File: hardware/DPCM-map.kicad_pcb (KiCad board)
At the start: 2 copper layers, 178 x 178 mm, 99 parts, among them J1 JMP, J2 Conn_01x06_Male, J3 Touch_Pad_+, J4 Touch_Pad_0, J5 Touch_Pad_-, J6 JMP, J7 SSD1306, P1 USB_C_Plug, Q1 2N7002, Q2 2N7002, SW1 SW_Push, SW2 SW_+_Fb, SW3 SW_0_Fb, SW4 SW_-_Fb, U1 AZ1117-3.3, U2 BME280, U4 ESP32-WROOM-32, U5 CH340G, Y1 12MHz

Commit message: routing optimization
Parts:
- moved R4 18.3 mm to (186.8, 180.5)
- moved C23 3.62 mm to (180.7, 70.0), turned to 270 degrees
- moved C37 0.28 mm to (157.6, 167.7), turned to 180 degrees
- turned R5 to 180 degrees
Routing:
- net LDR: track 105.3 -> 80.8 mm, vias 1 -> 2
- net +3V3: track 288.5 -> 269.0 mm
- net GND: track 98.2 -> 114.8 mm, vias 25 -> 40
- net SDA: track 181.4 -> 178.4 mm, vias 2 -> 4
- net LED_CHAIN: track 87.9 -> 90.4 mm
- net +5V: track 588.2 -> 585.8 mm, vias 0 -> 9
- net SCL: track 183.9 -> 182.0 mm
- net TOUCH_0: track 139.3 -> 141.0 mm
- net TOUCH_+: track 189.5 -> 191.1 mm
- net WIFI_RESET: track 60.3 -> 61.8 mm
- net Net-(D7-Pad2): track 18.8 -> 19.9 mm
- net RX: track 116.1 -> 115.2 mm
- net BOOT0: track 85.2 -> 86.1 mm
- net Net-(D19-Pad2): track 27.1 -> 26.4 mm, vias 0 -> 2
- net Net-(D22-Pad2): track 72.0 -> 72.2 mm, vias 0 -> 2
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
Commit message: move oled, change tracks
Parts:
- added G***: LOGO, map_edges_keepout:oled_display, F.Cu at (170.3, 211.3)
- moved J7 106.7 mm to (166.4, 199.1), turned to 270 degrees
- moved JP3 101.8 mm to (169.0, 194.0), turned to 90 degrees
- moved C13 101.7 mm to (171.1, 193.2), turned to 270 degrees
- moved C3 99.8 mm to (172.7, 193.2), turned to 270 degrees
- moved JP1 99.6 mm to (165.9, 194.1), turned to 90 degrees
- moved C6 97.8 mm to (163.8, 193.2), turned to 270 degrees
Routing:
- net +3V3: track 269.0 -> 180.4 mm, vias 4 -> 2
- net SDA: track 178.4 -> 119.9 mm, vias 4 -> 2
- net SCL: track 182.0 -> 133.5 mm
- net +5V: track 585.8 -> 591.6 mm
- net LDR: track 80.8 -> 83.6 mm
- net GND: track 114.8 -> 117.1 mm
- net Net-(D21-Pad2): track 48.6 -> 50.6 mm

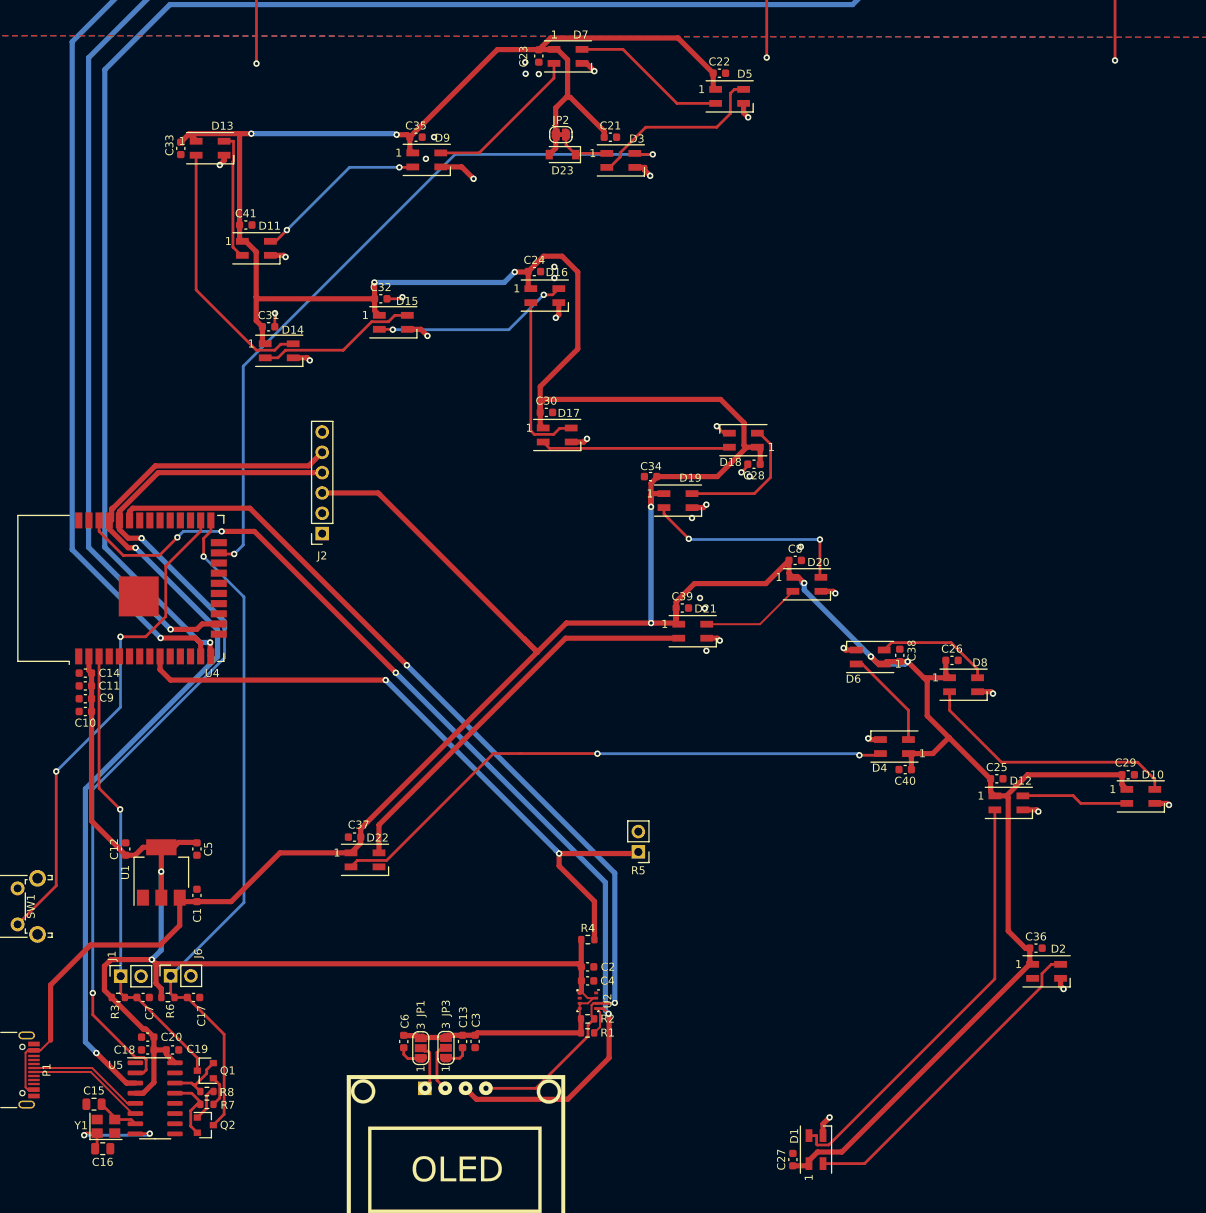
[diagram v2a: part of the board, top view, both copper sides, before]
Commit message: optimize routing under ESP, gnd plane, OLED position
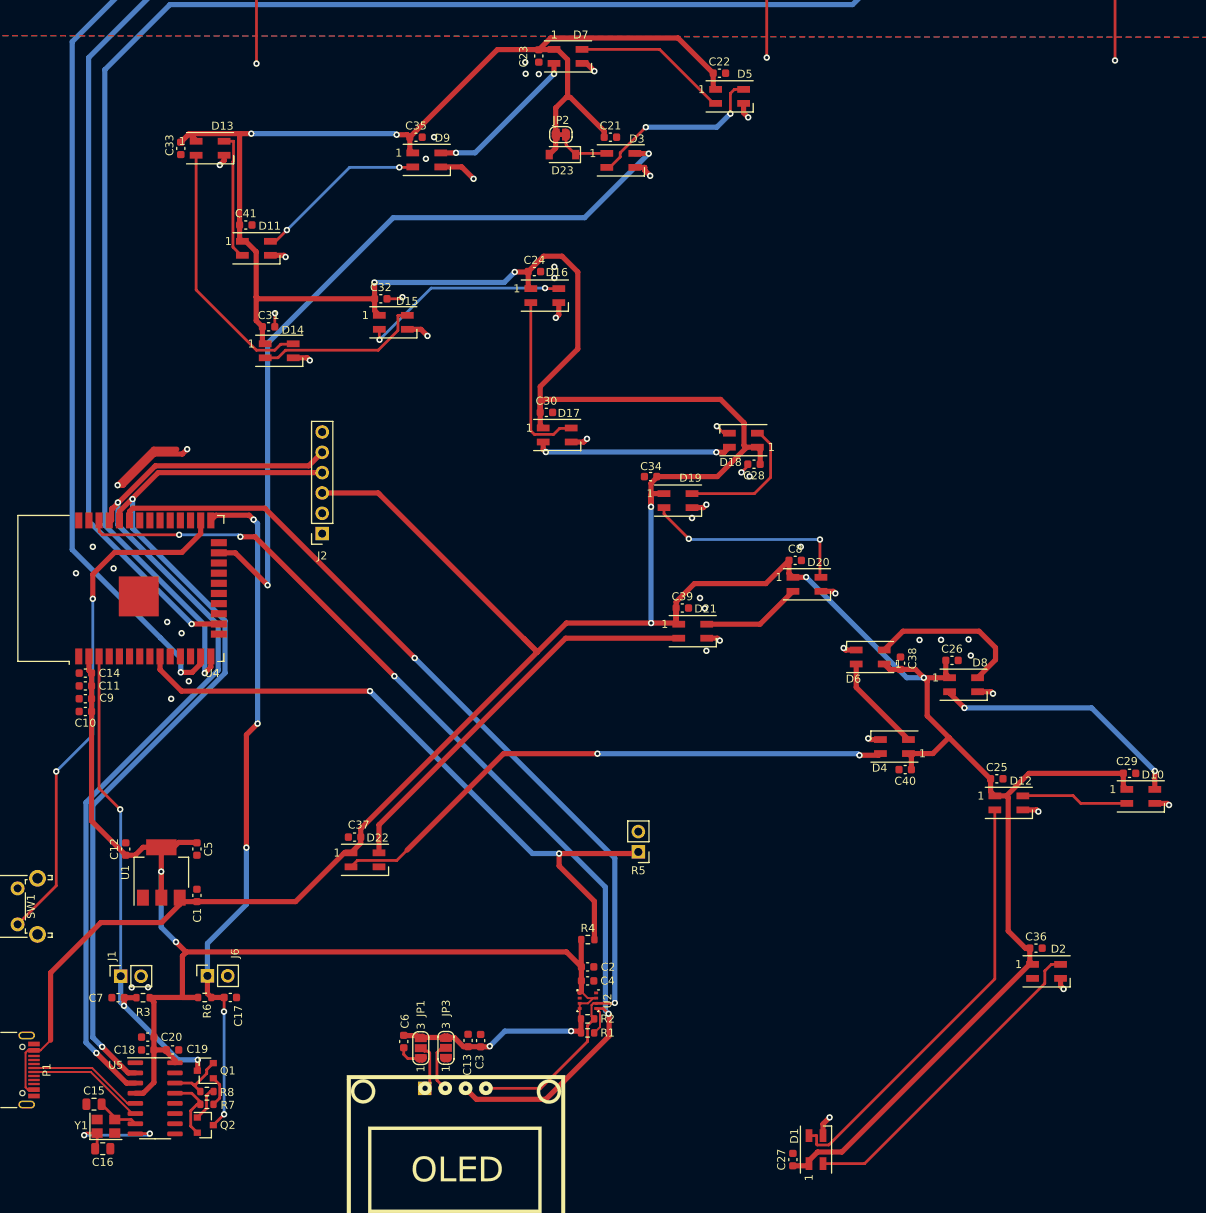
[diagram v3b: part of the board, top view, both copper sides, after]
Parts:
- moved C17 4.60 mm to (142.1, 187.7)
- moved J6 4.60 mm to (139.2, 185.0)
- moved R6 4.60 mm to (138.9, 187.7)
- moved C7 3.13 mm to (128.1, 187.8), turned to 180 degrees
- moved R3 3.09 mm to (131.2, 187.8), turned to 180 degrees
- moved C38 0.98 mm to (225.9, 145.9)
- moved C13 0.70 mm to (171.8, 193.1), turned to 90 degrees
- moved C3 0.70 mm to (173.4, 193.1), turned to 90 degrees
- moved C29 0.24 mm to (254.5, 159.7)
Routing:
- net GND: track 117.1 -> 133.8 mm, vias 40 -> 55
- net LED_CHAIN: track 90.4 -> 97.2 mm
- net +3V3: track 180.4 -> 174.3 mm, vias 2 -> 4
- net Net-(D6-Pad2): track 14.5 -> 20.4 mm
- net SCL: track 133.5 -> 129.1 mm
- net TOUCH_+: track 191.1 -> 194.5 mm
- net EN: track 57.8 -> 60.9 mm, vias 1 -> 3
- net WIFI_RESET: track 61.8 -> 64.9 mm
- net TOUCH_0: track 141.0 -> 138.5 mm
- net TOUCH_-: track 104.6 -> 106.9 mm
- net Net-(D15-Pad2): track 24.6 -> 26.4 mm
- net SDA: track 119.9 -> 121.4 mm
- net TX: track 117.5 -> 118.8 mm
- net Net-(D14-Pad2): track 20.0 -> 21.1 mm
- net Net-(D17-Pad2): track 23.7 -> 24.6 mm, vias 0 -> 2
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
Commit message: layout properly sminchied for the happiness of giacomo
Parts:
- removed the G*** at (170.3, 211.3)
- removed REF** (x4): MountingHole_4mm, MountingHole:MountingHole_4mm
- added H1: MountingHole_Pad, MountingHole:MountingHole_4mm_Pad_Via, F.Cu at (120.5, 60.0)
- added H2: MountingHole_Pad, MountingHole:MountingHole_4mm_Pad_Via, F.Cu at (120.5, 218.0)
- added H3: MountingHole_Pad, MountingHole:MountingHole_4mm_Pad_Via, F.Cu at (278.5, 60.0)
- added H4: MountingHole_Pad, MountingHole:MountingHole_4mm_Pad_Via, F.Cu at (278.5, 218.0)
- C2: value 10u -> 1u
- J7: value SSD1306 -> Conn_01x06_Female; footprint Connector_PinHeader_2.54mm:PinHeader_1x04_P2.54mm_Vertical -> Connector_PinHeader_2.54mm:PinHeader_1x06_P2.54mm_Vertical; moved to F.Cu
- U2: moved to B.Cu
- moved J2 86.6 mm to (74.0, 164.0)
- moved JP2 3.57 mm to (185.3, 82.9)
- moved C34 3.38 mm to (198.0, 122.8), turned to 0 degrees
- moved D23 3.33 mm to (185.4, 85.2)
- moved C31 2.83 mm to (149.7, 104.0)
- moved J7 2.48 mm to (164.0, 199.8), turned to 90 degrees
- moved C32 1.62 mm to (159.6, 101.3)
- moved D14 0.95 mm to (149.2, 106.8)
- moved D15 0.91 mm to (162.6, 104.2)
- moved U4 0.38 mm to (131.0, 136.5)
- turned U2 to 90 degrees
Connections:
- D2 pad 2: (no net) -> Net-(D2-Pad2)
- J2 pad 1: (no net) -> Net-(J2-Pad1)
- J2 pad 2: (no net) -> Net-(J2-Pad2)
- J2 pad 3: +5V -> +3V3
- P1 pad A5: (no net) -> Net-(P1-PadA5)
- P1 pad A8: (no net) -> Net-(P1-PadA8)
- P1 pad B5: (no net) -> Net-(P1-PadB5)
- P1 pad B8: (no net) -> Net-(P1-PadB8)
- U4 pad 10: (no net) -> Net-(U4-Pad10)
- U4 pad 11: (no net) -> Net-(U4-Pad11)
- U4 pad 12: (no net) -> Net-(U4-Pad12)
- U4 pad 17: (no net) -> Net-(U4-Pad17)
- U4 pad 18: (no net) -> Net-(U4-Pad18)
- U4 pad 19: (no net) -> Net-(U4-Pad19)
- U4 pad 20: (no net) -> Net-(U4-Pad20)
- U4 pad 21: (no net) -> Net-(U4-Pad21)
- U4 pad 22: (no net) -> Net-(U4-Pad22)
- U4 pad 24: (no net) -> Net-(U4-Pad24)
- U4 pad 27: (no net) -> Net-(U4-Pad27)
- U4 pad 28: (no net) -> Net-(U4-Pad28)
- U4 pad 29: (no net) -> Net-(U4-Pad29)
- U4 pad 30: (no net) -> Net-(U4-Pad30)
- U4 pad 31: (no net) -> Net-(U4-Pad31)
- U4 pad 32: (no net) -> Net-(U4-Pad32)
- U4 pad 37: (no net) -> Net-(U4-Pad37)
- U4 pad 4: (no net) -> Net-(U4-Pad4)
- U4 pad 5: (no net) -> Net-(U4-Pad5)
- U4 pad 6: (no net) -> Net-(U4-Pad6)
- U4 pad 7: (no net) -> Net-(U4-Pad7)
- U4 pad 8: (no net) -> Net-(U4-Pad8)
- U5 pad 10: (no net) -> Net-(U5-Pad10)
- U5 pad 11: (no net) -> Net-(U5-Pad11)
- U5 pad 12: (no net) -> Net-(U5-Pad12)
- U5 pad 15: (no net) -> Net-(U5-Pad15)
- U5 pad 9: (no net) -> Net-(U5-Pad9)
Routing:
- net +5V: track 590.9 -> 0.00 mm, vias 8 -> 0
- net TOUCH_+: track 194.5 -> 0.00 mm, vias 50 -> 0
- net +3V3: track 174.3 -> 0.00 mm, vias 4 -> 0
- net TOUCH_0: track 138.5 -> 0.00 mm, vias 57 -> 0
- net GND: track 133.8 -> 0.00 mm, vias 55 -> 0
- net SCL: track 129.1 -> 0.00 mm, vias 4 -> 0
- net SDA: track 121.4 -> 0.00 mm, vias 2 -> 0
- net TX: track 118.8 -> 0.00 mm, vias 2 -> 0
- net RX: track 114.6 -> 0.00 mm, vias 2 -> 0
- net TOUCH_-: track 106.9 -> 0.00 mm, vias 50 -> 0
- net LED_CHAIN: track 97.2 -> 0.00 mm, vias 2 -> 0
- net BOOT0: track 86.7 -> 0.00 mm, vias 5 -> 0
- net LDR: track 83.6 -> 0.00 mm, vias 2 -> 0
- net Net-(D22-Pad2): track 72.2 -> 0.00 mm, vias 2 -> 0
- net WIFI_RESET: track 64.9 -> 0.00 mm, vias 2 -> 0
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- added copper zone on F.Cu, net +3V3
- added copper zone on F.Cu, net +5V
- removed copper zone on F.Cu, net GND

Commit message: second fucking routing for the joy of balerio
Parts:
- U2: moved to F.Cu
- moved J2 66.2 mm to (134.0, 191.9), turned to 270 degrees
- moved R4 62.8 mm to (132.9, 148.1), turned to 90 degrees
- moved C27 37.7 mm to (241.9, 184.5)
- moved D1 37.7 mm to (244.8, 183.3)
- moved C36 34.8 mm to (216.1, 203.9)
- moved D2 34.8 mm to (217.4, 206.8)
- moved R5 31.8 mm to (173.3, 144.7)
- moved C41 14.1 mm to (138.7, 78.1)
- moved D11 14.1 mm to (140.1, 81.0)
- moved D13 13.0 mm to (144.9, 93.4)
- moved C33 11.9 mm to (143.9, 90.4), turned to 0 degrees
- moved D23 11.5 mm to (196.2, 81.0), turned to 0 degrees
- moved JP2 11.1 mm to (196.4, 83.3), turned to 180 degrees
- moved C32 8.05 mm to (165.3, 106.9), turned to 180 degrees
- moved C18 7.05 mm to (138.8, 194.5)
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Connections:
- D2 pad 2: Net-(D2-Pad2) -> (no net)
- J2 pad 1: Net-(J2-Pad1) -> (no net)
- J2 pad 2: Net-(J2-Pad2) -> (no net)
- P1 pad A5: Net-(P1-PadA5) -> (no net)
- P1 pad A8: Net-(P1-PadA8) -> (no net)
- P1 pad B5: Net-(P1-PadB5) -> (no net)
- P1 pad B8: Net-(P1-PadB8) -> (no net)
- U4 pad 10: Net-(U4-Pad10) -> (no net)
- U4 pad 11: Net-(U4-Pad11) -> (no net)
- U4 pad 12: Net-(U4-Pad12) -> (no net)
- U4 pad 17: Net-(U4-Pad17) -> (no net)
- U4 pad 18: Net-(U4-Pad18) -> (no net)
- U4 pad 19: Net-(U4-Pad19) -> (no net)
- U4 pad 20: Net-(U4-Pad20) -> (no net)
- U4 pad 21: Net-(U4-Pad21) -> (no net)
- U4 pad 22: Net-(U4-Pad22) -> (no net)
- U4 pad 24: Net-(U4-Pad24) -> (no net)
- U4 pad 27: Net-(U4-Pad27) -> (no net)
- U4 pad 28: Net-(U4-Pad28) -> (no net)
- U4 pad 29: Net-(U4-Pad29) -> (no net)
- U4 pad 30: Net-(U4-Pad30) -> (no net)
- U4 pad 31: Net-(U4-Pad31) -> (no net)
- U4 pad 32: Net-(U4-Pad32) -> (no net)
- U4 pad 37: Net-(U4-Pad37) -> (no net)
- U4 pad 4: Net-(U4-Pad4) -> (no net)
- U4 pad 5: Net-(U4-Pad5) -> (no net)
- U4 pad 6: Net-(U4-Pad6) -> (no net)
- U4 pad 7: Net-(U4-Pad7) -> (no net)
- U4 pad 8: Net-(U4-Pad8) -> (no net)
- U5 pad 10: Net-(U5-Pad10) -> (no net)
- U5 pad 11: Net-(U5-Pad11) -> (no net)
- U5 pad 12: Net-(U5-Pad12) -> (no net)
- U5 pad 15: Net-(U5-Pad15) -> (no net)
- U5 pad 9: Net-(U5-Pad9) -> (no net)
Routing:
- net GND: track 0.00 -> 333.7 mm, vias 0 -> 53
- net TOUCH_+: track 0.00 -> 157.0 mm
- net +3V3: track 0.00 -> 149.5 mm, vias 0 -> 8
- net TOUCH_0: track 0.00 -> 105.9 mm
- net +5V: track 0.00 -> 92.6 mm, vias 0 -> 6
- net Net-(D22-Pad2): track 0.00 -> 69.6 mm, vias 0 -> 2
- net TOUCH_-: track 0.00 -> 64.2 mm
- net LED_CHAIN: track 0.00 -> 58.1 mm, vias 0 -> 1
- net Net-(D21-Pad2): track 0.00 -> 51.5 mm, vias 0 -> 2
- net LDR: track 0.00 -> 43.7 mm
- net Net-(D1-Pad2): track 0.00 -> 36.1 mm
- net Net-(D10-Pad4): track 0.00 -> 32.8 mm
- net SDA: track 0.00 -> 26.8 mm
- net SCL: track 0.00 -> 26.2 mm
- net EN: track 0.00 -> 25.7 mm
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- added copper zone on F.Cu, net GND
- removed copper zone on F.Cu, net +3V3

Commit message: dio stracane se sto sbroglio non va bene Maria io esco
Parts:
- added C42: 10u, Capacitor_SMD:C_0603_1608Metric, F.Cu at (136.8, 148.0)
- added C43: 10u, Capacitor_SMD:C_0603_1608Metric, F.Cu at (136.8, 151.1)
- moved C15 8.48 mm to (139.1, 206.2), turned to 90 degrees
- moved C26 6.62 mm to (235.1, 151.6), turned to 180 degrees
- moved C18 4.46 mm to (143.1, 195.6)
- moved C19 4.46 mm to (146.2, 195.6)
- moved C20 4.46 mm to (143.1, 194.0)
- moved J1 4.46 mm to (132.7, 186.1)
- moved J2 4.46 mm to (138.3, 193.0)
- moved J6 4.46 mm to (143.6, 186.1)
- moved Q1 4.46 mm to (150.3, 198.2)
- moved Q2 4.46 mm to (150.3, 205.0)
- moved R6 4.46 mm to (143.2, 188.8)
- moved C7 4.46 mm to (132.4, 188.8)
- moved R3 4.46 mm to (135.5, 188.8)
- moved R7 4.46 mm to (150.5, 202.4)
- moved R8 4.46 mm to (150.5, 200.8)
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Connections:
- U4 pad 13: TOUCH_- -> (no net)
- U4 pad 14: TOUCH_+ -> (no net)
- U4 pad 16: TOUCH_0 -> (no net)
- U4 pad 23: LED_CHAIN -> TOUCH_+
- U4 pad 24: (no net) -> TOUCH_0
- U4 pad 26: WIFI_RESET -> TOUCH_-
- U4 pad 29: (no net) -> LED_CHAIN
- U4 pad 8: (no net) -> WIFI_RESET
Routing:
- net SCL: track 26.2 -> 123.0 mm, vias 0 -> 1
- net SDA: track 26.8 -> 122.1 mm, vias 0 -> 1
- net +5V: track 92.6 -> 177.5 mm
- net RX: track 13.2 -> 82.7 mm, vias 0 -> 2
- net TX: track 16.2 -> 84.5 mm, vias 0 -> 2
- net BOOT0: track 24.3 -> 86.1 mm, vias 0 -> 1
- net +3V3: track 149.5 -> 203.3 mm, vias 8 -> 10
- net WIFI_RESET: track 0.00 -> 50.7 mm, vias 0 -> 1
- net EN: track 25.7 -> 69.9 mm, vias 0 -> 2
- net LED_CHAIN: track 58.1 -> 85.3 mm, vias 1 -> 4
- net TOUCH_+: track 157.0 -> 184.1 mm
- net TOUCH_0: track 105.9 -> 128.0 mm
- net TOUCH_-: track 64.2 -> 85.9 mm
- net GND: track 333.7 -> 348.5 mm
- net Net-(D6-Pad2): track 16.4 -> 10.0 mm
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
